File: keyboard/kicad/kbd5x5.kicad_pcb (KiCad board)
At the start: 2 copper layers, 100 x 100 mm, 50 parts, among them SW1 mykbd, SW10 mykbd, SW11 mykbd, SW12 mykbd, SW13 mykbd, SW14 mykbd, SW15 mykbd, SW16 mykbd, SW17 mykbd, SW18 mykbd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

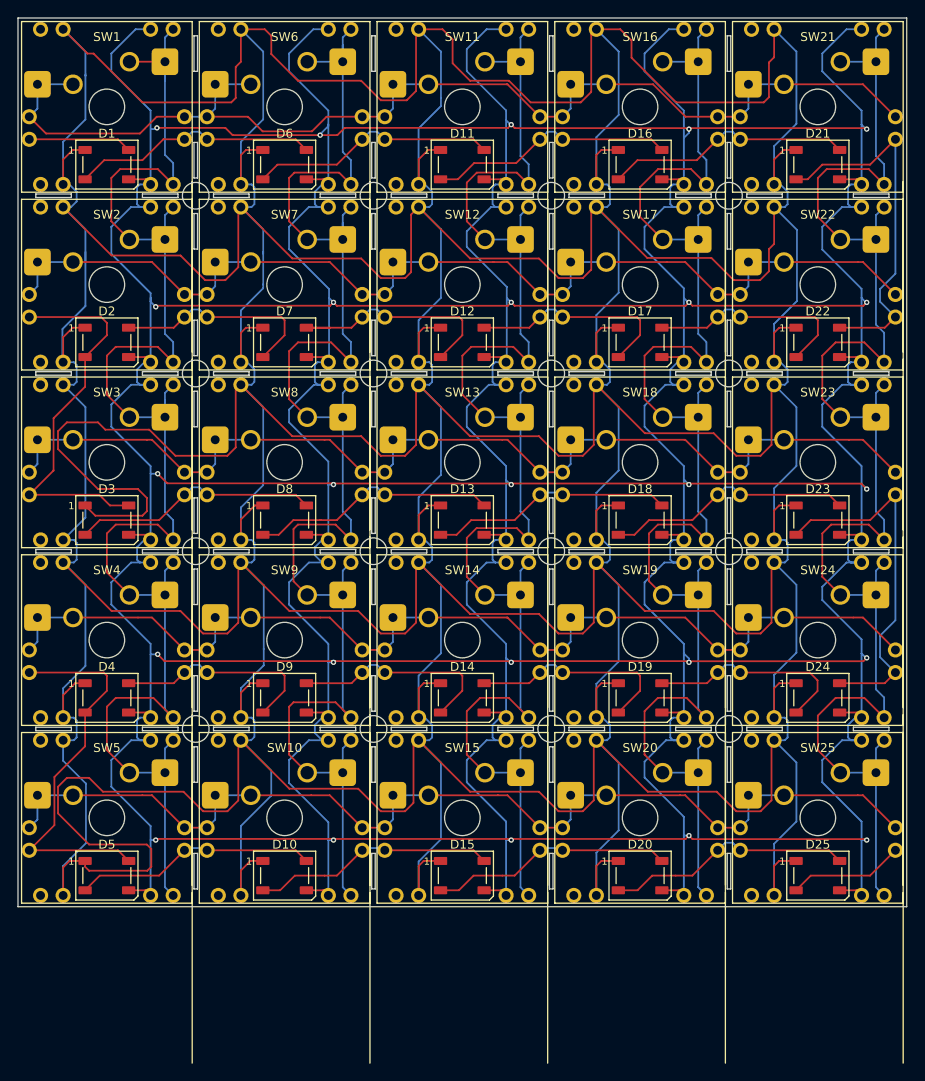
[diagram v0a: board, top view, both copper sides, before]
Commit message: keyboard: pinout align with 2.54mm Perforated circuit board
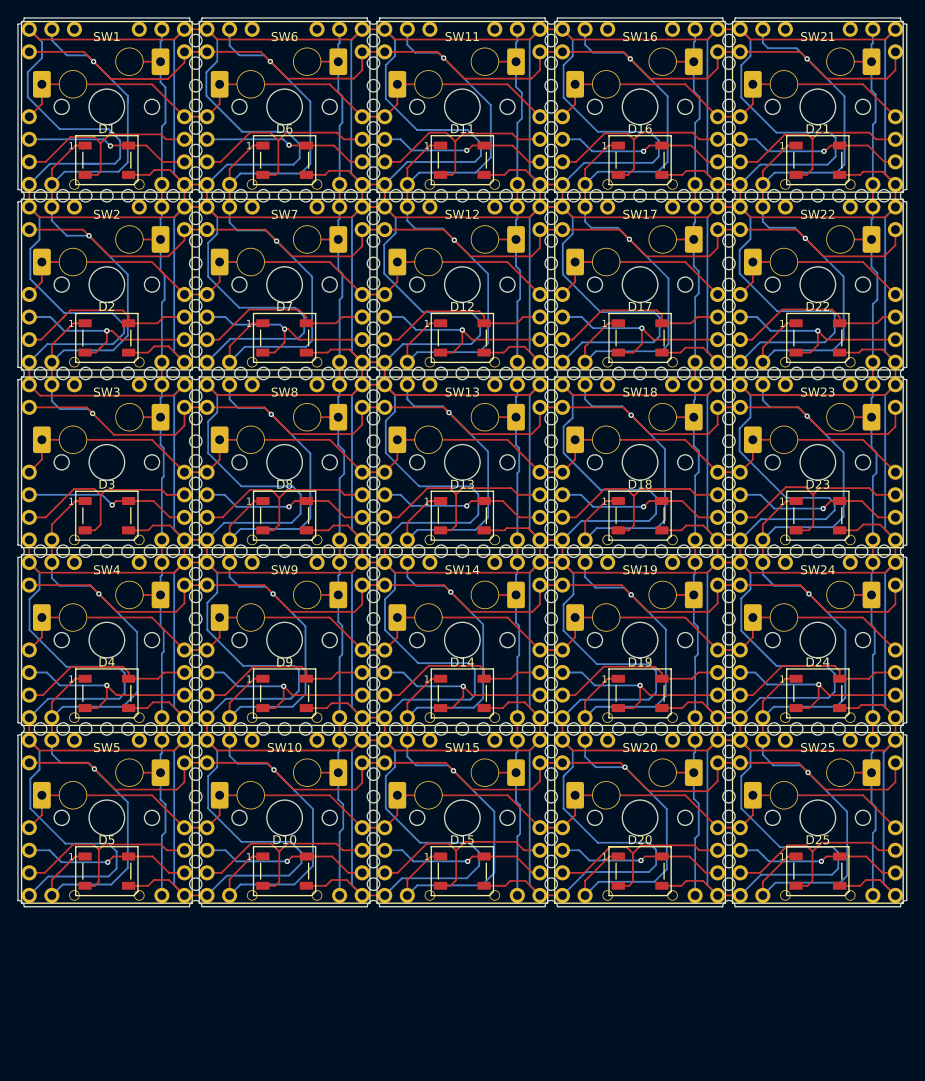
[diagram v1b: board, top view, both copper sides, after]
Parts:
- moved D1 0.50 mm to (40.0, 46.0)
- moved D10 0.50 mm to (60.0, 126.0)
- moved D11 0.50 mm to (80.0, 46.0)
- moved D12 0.50 mm to (80.0, 66.0)
- moved D13 0.50 mm to (80.0, 86.0)
- moved D14 0.50 mm to (80.0, 106.0)
- moved D15 0.50 mm to (80.0, 126.0)
- moved D16 0.50 mm to (100.0, 46.0)
- moved D17 0.50 mm to (100.0, 66.0)
- moved D18 0.50 mm to (100.0, 86.0)
- moved D19 0.50 mm to (100.0, 106.0)
- moved D2 0.50 mm to (40.0, 66.0)
- moved D20 0.50 mm to (100.0, 126.0)
- moved D21 0.50 mm to (120.0, 46.0)
- moved D22 0.50 mm to (120.0, 66.0)
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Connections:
- D15 pad 4: Net-(D10-DOUT) -> Net-(D15-DIN)
- D16 pad 4: Net-(D11-DOUT) -> Net-(D16-DIN)
- D17 pad 2: Net-(D12-DIN) -> Net-(D17-DOUT)
- D19 pad 2: Net-(D14-DIN) -> Net-(D19-DOUT)
- D20 pad 4: Net-(D15-DOUT) -> Net-(D20-DIN)
- D21 pad 4: Net-(D16-DOUT) -> Net-(D21-DIN)
- D22 pad 2: Net-(D17-DIN) -> Net-(D22-DOUT)
- D22 pad 4: Net-(D21-DOUT) -> Net-(D22-DIN)
- D24 pad 2: Net-(D19-DIN) -> Net-(D24-DOUT)
- D24 pad 4: Net-(D23-DOUT) -> Net-(D24-DIN)
- D25 pad 4: Net-(D20-DOUT) -> Net-(D25-DIN)
- D3 pad 4: Net-(D2-DOUT) -> Net-(D3-DIN)
- D5 pad 2: Net-(D10-DIN) -> Net-(D5-DOUT)
- D5 pad 4: Net-(D4-DOUT) -> Net-(D5-DIN)
- D6 pad 2: Net-(D11-DIN) -> Net-(D6-DOUT)
- D6 pad 4: Net-(D1-DOUT) -> Net-(D6-DIN)
- D7 pad 2: Net-(D2-DIN) -> Net-(D7-DOUT)
- D7 pad 4: Net-(D12-DOUT) -> Net-(D7-DIN)
- D9 pad 2: Net-(D4-DIN) -> Net-(D9-DOUT)
- D9 pad 4: Net-(D14-DOUT) -> Net-(D9-DIN)
- SW15 pad 3: Net-(D10-DOUT) -> Net-(D15-DIN)
- SW16 pad 3: Net-(D11-DOUT) -> Net-(D16-DIN)
- SW17 pad 3: Net-(D12-DIN) -> Net-(D17-DOUT)
- SW19 pad 3: Net-(D14-DIN) -> Net-(D19-DOUT)
- SW20 pad 3: Net-(D15-DOUT) -> Net-(D20-DIN)
- SW21 pad 3: Net-(D16-DOUT) -> Net-(D21-DIN)
- SW22 pad 3: Net-(D17-DIN) -> Net-(D22-DOUT)
- SW22 pad 4: Net-(D21-DOUT) -> Net-(D22-DIN)
- SW24 pad 3: Net-(D19-DIN) -> Net-(D24-DOUT)
- SW24 pad 4: Net-(D23-DOUT) -> Net-(D24-DIN)
- SW25 pad 3: Net-(D20-DOUT) -> Net-(D25-DIN)
- SW3 pad 3: Net-(D2-DOUT) -> Net-(D3-DIN)
- SW5 pad 3: Net-(D4-DOUT) -> Net-(D5-DIN)
- SW5 pad 4: Net-(D10-DIN) -> Net-(D5-DOUT)
- SW6 pad 3: Net-(D1-DOUT) -> Net-(D6-DIN)
- SW6 pad 4: Net-(D11-DIN) -> Net-(D6-DOUT)
- SW7 pad 3: Net-(D2-DIN) -> Net-(D7-DOUT)
- SW7 pad 4: Net-(D12-DOUT) -> Net-(D7-DIN)
- SW9 pad 3: Net-(D4-DIN) -> Net-(D9-DOUT)
- SW9 pad 4: Net-(D14-DOUT) -> Net-(D9-DIN)
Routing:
- net GND: track 1146.2 -> 2101.5 mm, vias 25 -> 0
- net VCC: track 1396.4 -> 1520.9 mm, vias 0 -> 25
- net Net-(SW1-Pad2): track 181.4 -> 116.9 mm
- net Net-(SW10-Pad2): track 178.6 -> 117.1 mm
- net Net-(SW11-Pad2): track 174.4 -> 114.3 mm
- net Net-(SW16-Pad2): track 176.9 -> 117.3 mm
- net Net-(SW21-Pad2): track 176.5 -> 117.0 mm
- net Net-(D6-DOUT): track 0.00 -> 25.2 mm
- net Net-(D5-DOUT): track 0.00 -> 24.9 mm
- net Net-(D17-DOUT): track 0.00 -> 23.4 mm, vias 0 -> 1
- net Net-(D24-DOUT): track 0.00 -> 23.1 mm, vias 0 -> 1
- net Net-(D19-DOUT): track 0.00 -> 23.1 mm, vias 0 -> 1
- net Net-(D7-DOUT): track 0.00 -> 22.9 mm, vias 0 -> 1
- net Net-(D22-DOUT): track 0.00 -> 22.9 mm, vias 0 -> 1
- net Net-(D9-DOUT): track 0.00 -> 22.8 mm, vias 0 -> 1
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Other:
- outline, holes or cut-outs redrawn

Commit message: keyboard pcb: bottom board(esp32s3 minimal 20mmx40mm)
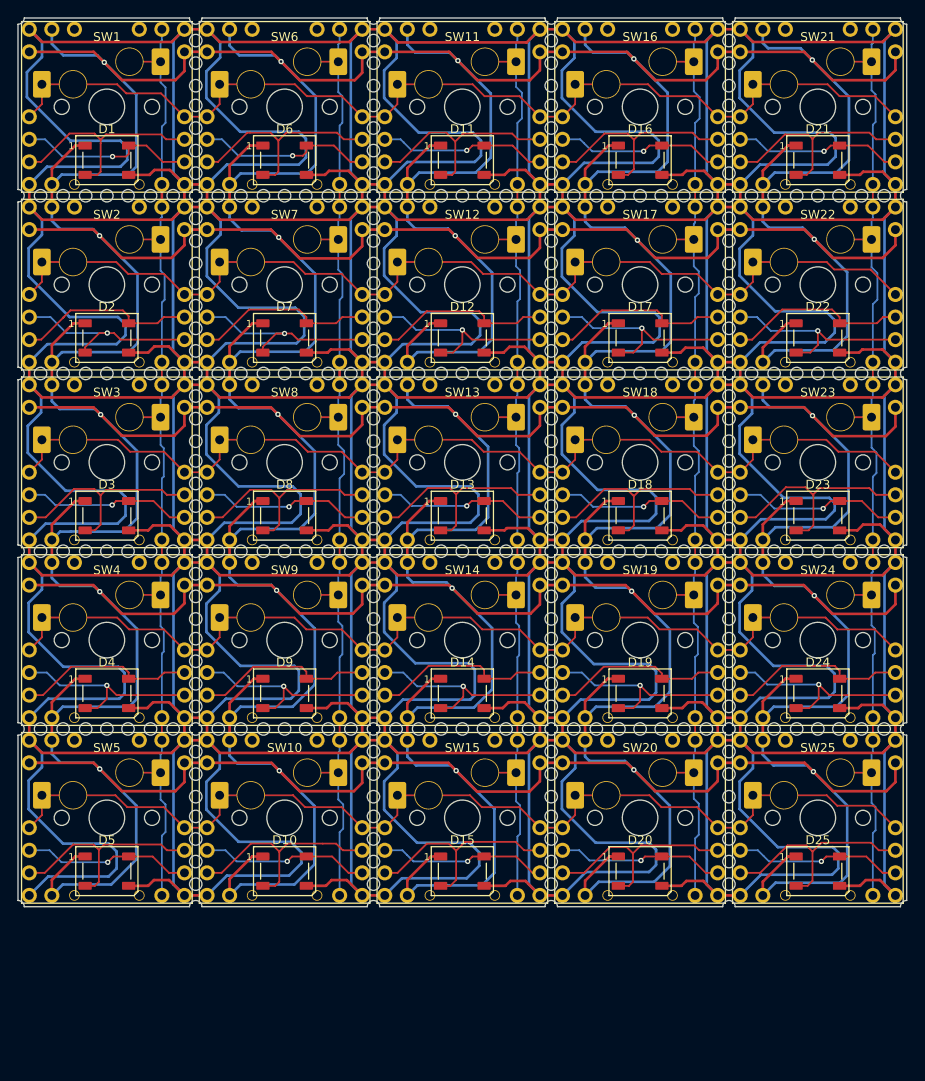
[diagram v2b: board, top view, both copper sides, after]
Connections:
- D18 pad 4: Net-(D13-DOUT) -> Net-(D18-DIN)
- D23 pad 4: Net-(D18-DOUT) -> Net-(D23-DIN)
- D8 pad 2: Net-(D13-DIN) -> Net-(D8-DOUT)
- D8 pad 4: Net-(D3-DOUT) -> Net-(D8-DIN)
- SW18 pad 3: Net-(D13-DOUT) -> Net-(D18-DIN)
- SW23 pad 3: Net-(D18-DOUT) -> Net-(D23-DIN)
- SW8 pad 3: Net-(D3-DOUT) -> Net-(D8-DIN)
- SW8 pad 4: Net-(D13-DIN) -> Net-(D8-DOUT)
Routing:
- net GND: track 2101.5 -> 2197.7 mm
- net VCC: track 1520.9 -> 1583.9 mm
- net Net-(D13-DIN): track 43.8 -> 19.0 mm
- net Net-(D8-DOUT): track 0.00 -> 24.8 mm
- net Net-(D18-DOUT): track 44.2 -> 25.0 mm, vias 1 -> 0
- net Net-(D23-DIN): track 0.00 -> 19.2 mm, vias 0 -> 1
- net Net-(D18-DIN): track 0.00 -> 19.1 mm, vias 0 -> 1
- net Net-(D13-DOUT): track 44.2 -> 25.2 mm, vias 1 -> 0
- net Net-(D8-DIN): track 0.00 -> 19.1 mm, vias 0 -> 1
- net Net-(D3-DOUT): track 43.9 -> 24.9 mm, vias 1 -> 0
- net Net-(SW12-Pad1): track 114.0 -> 119.9 mm
- net Net-(SW11-Pad2): track 114.3 -> 116.9 mm
- net Net-(SW1-Pad1): track 116.6 -> 119.1 mm
- net Net-(D1-DIN): track 18.6 -> 20.1 mm
- net Net-(D6-DIN): track 18.5 -> 19.9 mm
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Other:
- outline, holes or cut-outs redrawn
